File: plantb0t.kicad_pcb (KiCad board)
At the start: 2 copper layers, 50 x 50 mm, 61 parts, among them P1 CONN_02X09, P10 CONN_01X01, P11 CONN_01X01, P12 CONN_01X01, P13 CONN_01X01, P2 USB_OTG, P3 CONN_02X03, P4 CONN_01X02, P5 CONN_01X02, P6 CONN_01X02, P7 CONN_01X02, P8 CONN_01X04, P9 CONN_01X04, Q1 BS170, Q2 BS170, SW1 SWITCH_INV, U1 ESP-12, U10 BMP280, U11 74HC(T)4051, U12 LEDx2, U2 CP2102, U3 ZXCL5213V30H5CT-ND, U4 MCP4017 100K, U5 FXL6408, U6 FC6946010R, U7 FC6946010R, U8 MCP6001, U9 PSSI2021SAY

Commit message: Tweaking the ground plane and fixing missing traces
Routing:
- net /SENSORS: track 13.2 -> 44.4 mm, vias 0 -> 4
- net /GPIO_1: track 48.2 -> 28.3 mm
- net GND: track 50.4 -> 65.5 mm, vias 2 -> 4
- net +3V3: track 199.7 -> 205.8 mm, vias 8 -> 10
- added copper zone on B.Cu, net GND
- added copper zone on F.Cu, net GND
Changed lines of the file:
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@@
     (thickness 1.6)
     (drawings 8)
-    (tracks 735)
+    (tracks 768)
     (zones 0)
     (modules 61)
@@
   (gr_line (start 67 90) (end 113 90) (layer Edge.Cuts) (width 0.15))
   (gr_line (start 65 42) (end 65 88) (layer Edge.Cuts) (width 0.15))
+  (segment (start 87.75 78.95) (end 87.325736 78.95) (width 0.11) (layer F.Cu) (net 1))
+  (segment (start 87.325736 78.95) (end 86.025 78.95) (width 0.11) (layer F.Cu) (net 1))
+  (segment (start 84.275 79.825) (end 85.15 78.95) (width 0.11) (layer B.Cu) (net 1))
+  (segment (start 85.15 78.95) (end 87.75 78.95) (width 0.11) (layer B.Cu) (net 1))
+  (via (at 87.75 78.95) (size 0.6) (drill 0.4) (layers F.Cu B.Cu) (net 1))
+  (segment (start 83.13096 77.63) (end 83.99153 77.63) (width 0.11) (layer F.Cu) (net 1))
+  (segment (start 83.99153 77.63) (end 84.136531 77.775001) (width 0.11) (layer F.Cu) (net 1))
+  (via (at 84.275 79.825) (size 0.6) (drill 0.4) (layers F.Cu B.Cu) (net 1))
+  (segment (start 84.136531 77.775001) (end 84.136531 79.686531) (width 0.11) (layer F.Cu) (net 1))
+  (segment (start 84.136531 79.686531) (end 84.275 79.825) (width 0.11) (layer F.Cu) (net 1))
+  (segment (start 82.68 73.82) (end 82.04 73.82) (width 0.11) (layer F.Cu) (net 1))
+  (segment (start 82.04 73.82) (end 81.894999 73.674999) (width 0.11) (layer F.Cu) (net 1))
+  (segment (start 81.894999 73.674999) (end 81.894999 72.340999) (width 0.11) (layer F.Cu) (net 1))
+  (segment (start 81.894999 72.340999) (end 82.135997 72.100001) (width 0.11) (layer F.Cu) (net 1))
+  (segment (start 82.135997 72.100001) (end 84.600001 72.100001) (width 0.11) (layer F.Cu) (net 1))
+  (segment (start 86.2 72.6) (end 85.1 72.6) (width 0.11) (layer F.Cu) (net 1))
+  (segment (start 85.1 72.6) (end 84.9 72.4) (width 0.11) (layer F.Cu) (net 1))
   (segment (start 75.57 46.32) (end 75.57 45.18832) (width 0.175) (layer B.Cu) (net 1))
   (segment (start 75.57 45.18832) (end 74.88168 44.5) (width 0.175) (layer B.Cu) (net 1))
@@
   (segment (start 108.53 59.105) (end 108.53 59.175) (width 0.175) (layer F.Cu) (net 3))
   (segment (start 108.53 59.035) (end 108.53 59.105) (width 0.175) (layer F.Cu) (net 3))
+  (via (at 74.575 74.175) (size 0.6) (drill 0.4) (layers F.Cu B.Cu) (net 4))
+  (segment (start 75.17 74.77) (end 74.575 74.175) (width 0.11) (layer B.Cu) (net 4))
+  (segment (start 80.48 74.77) (end 75.17 74.77) (width 0.11) (layer B.Cu) (net 4))
+  (via (at 80.48 74.77) (size 0.6) (drill 0.4) (layers F.Cu B.Cu) (net 4))
   (segment (start 68.71 70) (end 68.71 71.221314) (width 0.25) (layer F.Cu) (net 4))
   (segment (start 68.71 71.221314) (end 70.138686 72.65) (width 0.25) (layer F.Cu) (net 4))
@@
   (segment (start 70.386401 63.243599) (end 71.25 62.38) (width 0.175) (layer F.Cu) (net 14))
   (segment (start 71.25 59.84) (end 72.113599 58.976401) (width 0.175) (layer F.Cu) (net 15))
-  (segment (start 80.922216 53.11317) (end 81.372896 52.66249) (width 0.175) (layer F.Cu) (net 15))
   (segment (start 72.113599 58.976401) (end 72.113599 58.140031) (width 0.175) (layer F.Cu) (net 15))
-  (segment (start 92.602692 55.5) (end 97.5 55.5) (width 0.175) (layer F.Cu) (net 15))
   (segment (start 72.113599 58.140031) (end 73.71363 56.54) (width 0.175) (layer F.Cu) (net 15))
   (segment (start 73.71363 56.54) (end 78.441411 56.54) (width 0.175) (layer F.Cu) (net 15))
   (segment (start 78.441411 56.54) (end 80.922216 54.059195) (width 0.175) (layer F.Cu) (net 15))
+  (segment (start 81.372896 52.66249) (end 84.865153 52.66249) (width 0.175) (layer F.Cu) (net 15))
+  (segment (start 84.865153 52.66249) (end 87.702663 55.5) (width 0.175) (layer F.Cu) (net 15))
   (segment (start 80.922216 54.059195) (end 80.922216 53.11317) (width 0.175) (layer F.Cu) (net 15))
-  (segment (start 81.372896 52.66249) (end 89.765182 52.66249) (width 0.175) (layer F.Cu) (net 15))
-  (segment (start 89.765182 52.66249) (end 92.602692 55.5) (width 0.175) (layer F.Cu) (net 15))
+  (segment (start 80.922216 53.11317) (end 81.372896 52.66249) (width 0.175) (layer F.Cu) (net 15))
+  (segment (start 87.702663 55.5) (end 97.5 55.5) (width 0.175) (layer F.Cu) (net 15))
   (segment (start 97.5 57.5) (end 98.084418 57.5) (width 0.175) (layer F.Cu) (net 16))
   (segment (start 78.887471 40.808899) (end 78.288899 41.407471) (width 0.175) (layer F.Cu) (net 16))
@@
   (segment (start 73.398904 55.151096) (end 72.113599 56.436401) (width 0.175) (layer F.Cu) (net 16))
   (segment (start 74.045269 45.651101) (end 73.398904 46.297466) (width 0.175) (layer F.Cu) (net 16))
-  (segment (start 108.45886 66.84) (end 106.9 66.84) (width 0.175) (layer F.Cu) (net 17))
   (segment (start 106.9 66.84) (end 100.991058 66.84) (width 0.175) (layer F.Cu) (net 17))
+  (segment (start 87.157888 55.87501) (end 84.782878 53.5) (width 0.175) (layer F.Cu) (net 17))
+  (segment (start 100.991058 66.84) (end 96.43 62.278942) (width 0.175) (layer F.Cu) (net 17))
+  (segment (start 96.43 62.278942) (end 96.43 58.04) (width 0.175) (layer F.Cu) (net 17))
+  (segment (start 96.43 58.04) (end 94.26501 55.87501) (width 0.175) (layer F.Cu) (net 17))
+  (segment (start 94.26501 55.87501) (end 87.157888 55.87501) (width 0.175) (layer F.Cu) (net 17))
+  (segment (start 84.782878 53.5) (end 83.5 53.5) (width 0.175) (layer F.Cu) (net 17))
+  (segment (start 108.45886 66.84) (end 106.9 66.84) (width 0.175) (layer F.Cu) (net 17))
   (segment (start 106.45 67.35) (end 106.45 66.99) (width 0.11) (layer F.Cu) (net 17))
   (segment (start 106.45 66.99) (end 106.6 66.84) (width 0.11) (layer F.Cu) (net 17))
@@
   (segment (start 67.464491 60.414382) (end 67.464491 58.545509) (width 0.175) (layer F.Cu) (net 17))
   (segment (start 67.464491 58.545509) (end 67.846401 58.163599) (width 0.175) (layer F.Cu) (net 17))
-  (segment (start 92.447357 55.875009) (end 90.072348 53.5) (width 0.175) (layer F.Cu) (net 17))
-  (segment (start 90.072348 53.5) (end 83.5 53.5) (width 0.175) (layer F.Cu) (net 17))
-  (segment (start 96.43 58.04) (end 94.26501 55.87501) (width 0.175) (layer F.Cu) (net 17))
-  (segment (start 94.26501 55.87501) (end 92.447357 55.875009) (width 0.175) (layer F.Cu) (net 17))
-  (segment (start 96.43 62.278942) (end 96.43 58.04) (width 0.175) (layer F.Cu) (net 17))
-  (segment (start 100.991058 66.84) (end 96.43 62.278942) (width 0.175) (layer F.Cu) (net 17))
   (segment (start 100.11252 57.471898) (end 98.084418 59.5) (width 0.175) (layer F.Cu) (net 18))
   (segment (start 100.11252 54.997757) (end 100.11252 57.471898) (width 0.175) (layer F.Cu) (net 18))
@@
   (segment (start 82.68 72.87) (end 83.385 72.87) (width 0.175) (layer F.Cu) (net 62))
   (segment (start 83.385 72.87) (end 83.93 73.415) (width 0.175) (layer F.Cu) (net 62))
-  (segment (start 71.25 70) (end 91.108598 70) (width 0.11) (layer B.Cu) (net 68))
   (segment (start 96.487569 75.378971) (end 104.946029 75.378971) (width 0.11) (layer B.Cu) (net 68))
   (segment (start 91.108598 70) (end 96.487569 75.378971) (width 0.11) (layer B.Cu) (net 68))
@@
   (segment (start 66 50.8) (end 67.12 49.68) (width 0.175) (layer F.Cu) (net 70))
   (segment (start 67.12 49.68) (end 68.71 49.68) (width 0.175) (layer F.Cu) (net 70))
+  (segment (start 85.8 73.15) (end 84.18 74.77) (width 0.11) (layer B.Cu) (net 71))
+  (segment (start 84.18 74.77) (end 82.68 74.77) (width 0.11) (layer B.Cu) (net 71))
+  (via (at 82.68 74.77) (size 0.6) (drill 0.4) (layers F.Cu B.Cu) (net 71))
+  (segment (start 85.8 69.075) (end 85.8 73.15) (width 0.11) (layer B.Cu) (net 71))
+  (segment (start 85.8 60.5) (end 85.8 69.075) (width 0.11) (layer F.Cu) (net 71))
+  (via (at 85.8 69.075) (size 0.6) (drill 0.4) (layers F.Cu B.Cu) (net 71))
+  (segment (start 88.775 57.525) (end 85.8 60.5) (width 0.11) (layer F.Cu) (net 71))
+  (segment (start 88.725 54.075) (end 88.725 57.475) (width 0.11) (layer B.Cu) (net 71))
+  (segment (start 88.725 57.475) (end 88.775 57.525) (width 0.11) (layer B.Cu) (net 71))
+  (via (at 88.775 57.525) (size 0.6) (drill 0.4) (layers F.Cu B.Cu) (net 71))
+  (segment (start 83.5 49.5) (end 84.15 49.5) (width 0.11) (layer F.Cu) (net 71))
+  (segment (start 84.15 49.5) (end 88.725 54.075) (width 0.11) (layer F.Cu) (net 71))
+  (via (at 88.725 54.075) (size 0.6) (drill 0.4) (layers F.Cu B.Cu) (net 71))
   (segment (start 82.68 75.27) (end 82.68 74.77) (width 0.175) (layer F.Cu) (net 71))
   (segment (start 82.035898 75.914102) (end 82.68 75.27) (width 0.175) (layer F.Cu) (net 71))
@@
       )
     )
+  )
+  (zone (net 1) (net_name GND) (layer F.Cu) (hatch edge 0.508)
+    (connect_pads (clearance 0.05))
+    (min_thickness 0.35)
+    (fill yes (arc_segments 16) (thermal_gap 0.005) (thermal_bridge_width 0.762))
+    (polygon
+      (pts
+        (xy 64.6 39.05) (xy 119.5 38) (xy 118.8 93.05) (xy 63.25 92.975)
+      )
+    )
+  )
+  (zone (net 1) (net_name GND) (layer B.Cu) (hatch edge 0.508)
+    (connect_pads (clearance 0.05))
+    (min_thickness 0.35)
+    (fill yes (arc_segments 16) (thermal_gap 0.005) (thermal_bridge_width 0.762))
+    (polygon
+      (pts
+        (xy 120.75 36.875) (xy 120.75 95.2) (xy 60.925 94.675) (xy 62.475 35.475) (xy 120.775 36.7)
+      )
+    )

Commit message: Finishing up board Revision A 2.0
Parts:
- I²C EXP 1: renamed from P8
- I²C EXP 2: renamed from P9
- moved FLASH 71.4 mm to (139.0, 90.4)
- moved R8 71.1 mm to (137.7, 81.3)
- moved D4 71.1 mm to (137.7, 84.9)
- moved R1 70.8 mm to (139.5, 84.5)
- moved D3 69.8 mm to (163.3, 92.7)
- moved U12 69.8 mm to (165.7, 89.2)
- moved AN_1 69.8 mm to (135.4, 120.8)
- moved AN_2 69.8 mm to (166.9, 120.8)
- moved AN_4 69.8 mm to (174.3, 109.2)
- moved C11 69.8 mm to (156.7, 99.7)
- moved C12 69.8 mm to (141.3, 102.8)
- moved C2 69.8 mm to (170.2, 82.5)
- moved C3 69.8 mm to (174.5, 81.0)
- moved C4 69.8 mm to (165.2, 75.8)
- moved C6 69.8 mm to (165.1, 98.0)
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- renumbered P7 to AN_1, P6 to AN_2, P5 to AN_3, P4 to AN_4, SW1 to FLASH, P3 to PROG, P2 to USB
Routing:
- net +5V: track 74.4 -> 81.5 mm
- net /GPIO_5: track 31.4 -> 34.1 mm
- net /GPIO_6: track 52.2 -> 54.4 mm
- net GND: track 65.5 -> 67.6 mm
- net /GPIO_7: track 54.9 -> 56.9 mm
- net /I2C_CLOCK: track 159.4 -> 158.3 mm
- net /SLEEP_CTRL: track 60.3 -> 59.2 mm
- net +3V3: track 205.8 -> 205.0 mm
- net /SENSORS: track 44.4 -> 45.2 mm
- net /CH_PD: track 22.3 -> 21.6 mm
- removed copper zone on F.Cu, net /PERM_3V3
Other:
- outline, holes or cut-outs redrawn
- board text added: "+5V"
- board text added: "10/2016"
- board text added: "3V3"
- board text added: "GND"
- board text added: "IO_2"
- board text added: "IO_3"
- board text added: "IO_4"
- board text added: "IO_5"
- board text added: "IO_6"
- board text added: "IO_7"
- board text added: "OUT_1"
- board text added: "Open Plantbot Rev A2"
- board text added: "P3V3"
- board text added: "RST"
- board text added: "SCL"
- board text added: "SDA"
- board text added: "SLP"

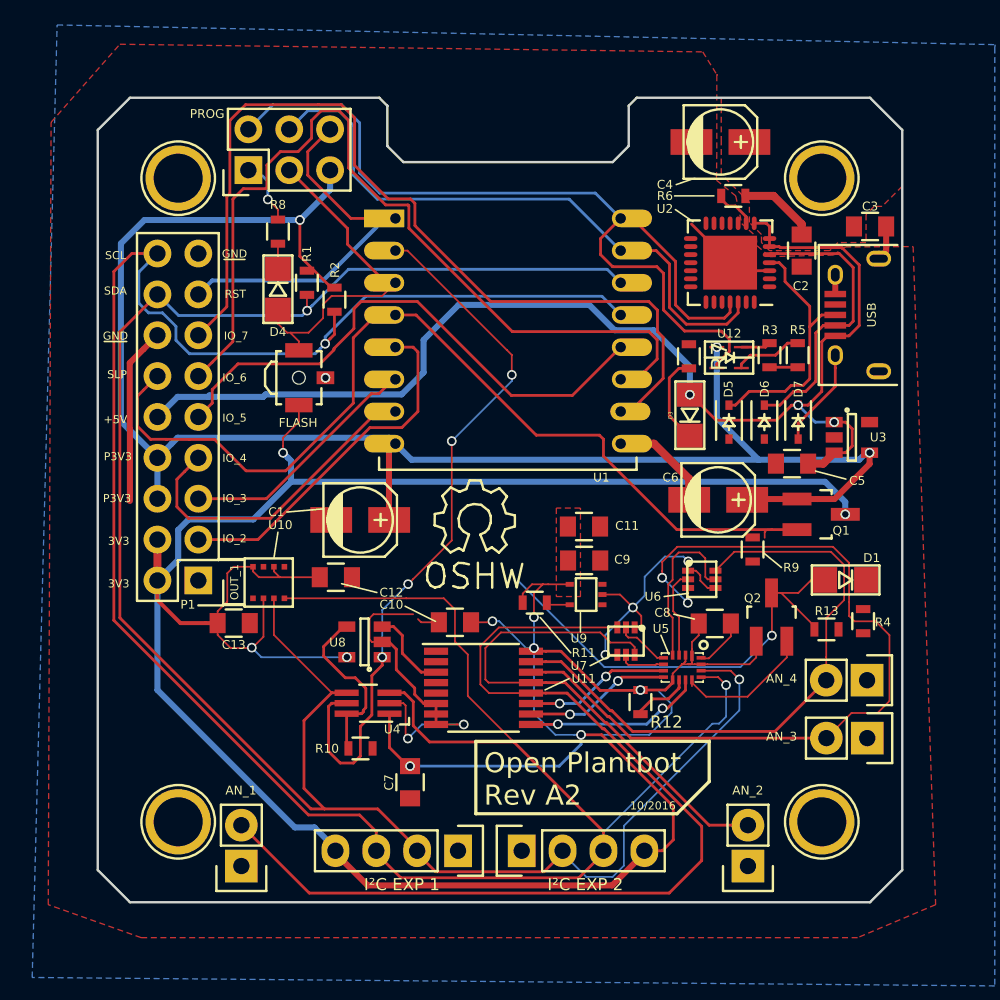
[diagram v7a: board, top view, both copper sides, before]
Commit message: Majorly updating the board. Moving some components. Changing the Plantbot logo \o/
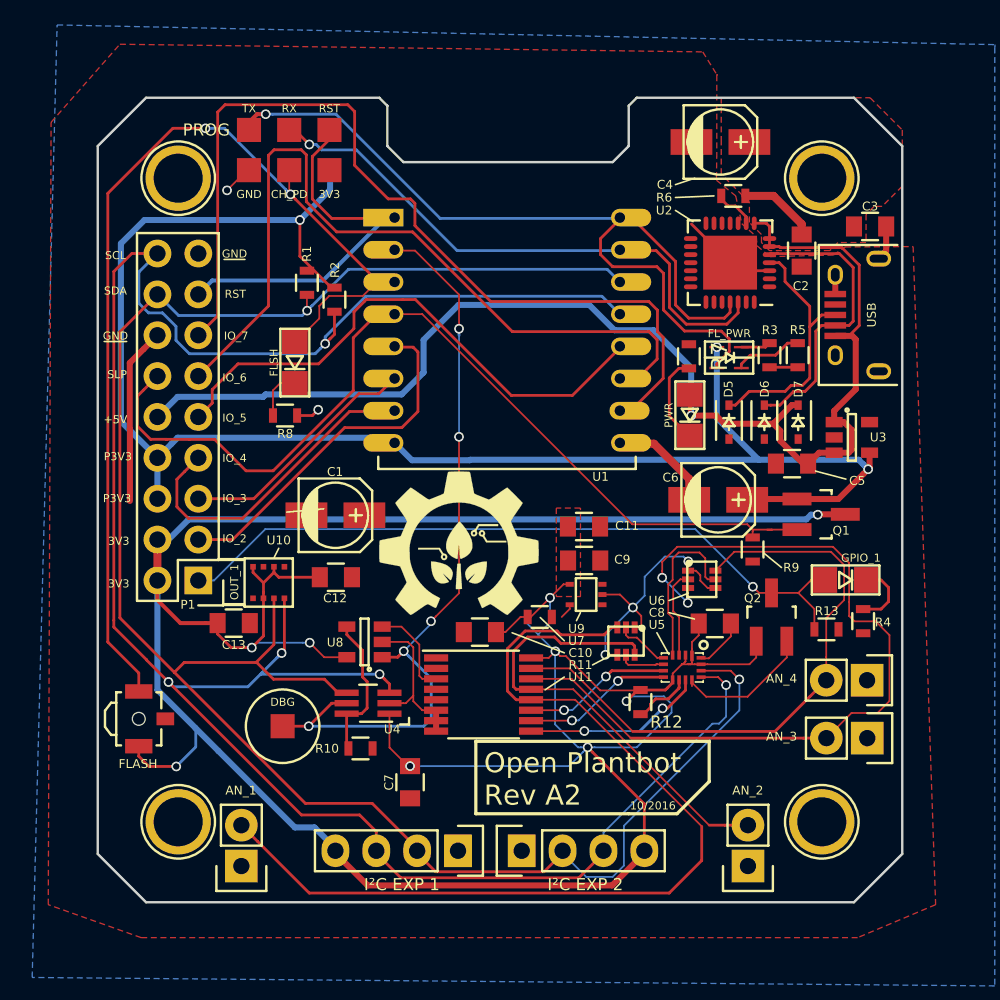
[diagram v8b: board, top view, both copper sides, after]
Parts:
- removed the PROG at (135.9, 77.5)
- removed REF**: Symbol_OSHW-Logo_SilkScreen, Symbols:Symbol_OSHW-Logo_SilkScreen
- added DBG: CONN_01X01, Connect:1pin, F.Cu at (138.0, 112.1)
- added G***: LOGO, plantbot_kicad:plantbot_icon, F.Cu at (148.9, 100.7)
- added G***: LOGO, eu_love:eu_love, B.Cu at (153.0, 103.5)
- added PROG: CONN_02X03, base_types:prog_6pin, F.Cu at (138.4, 77.5)
- moved FLASH 23.4 mm to (129.1, 111.6)
- moved R8 11.4 mm to (138.1, 92.8), turned to 180 degrees
- moved FLSH 4.68 mm to (138.8, 89.5), turned to 270 degrees
- moved C10 1.67 mm to (150.2, 106.2)
- moved C1 1.57 mm to (141.3, 99.0)
- moved R11 0.94 mm to (154.0, 105.3)
- moved U11 0.42 mm to (150.5, 110.1)
- moved U1 0.07 mm to (144.9, 80.5)
- renumbered D4 to FLSH, U12 to FL_PWR, D1 to GPIO_1, D3 to PWR
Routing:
- net /CH_PD: track 21.6 -> 65.3 mm, vias 0 -> 2
- net /I2C_CLOCK: track 158.3 -> 139.7 mm, vias 2 -> 5
- net GND: track 67.6 -> 49.1 mm, vias 4 -> 2
- net /GPIO_1: track 28.3 -> 45.4 mm
- net +3V3: track 205.0 -> 195.9 mm, vias 10 -> 9
- net +5V: track 81.5 -> 86.1 mm, vias 3 -> 1
- net /PERM_3V3: track 105.0 -> 100.6 mm
- net Net-(D1-Pad1): track 0.00 -> 4.23 mm
- net /GPIO_6: track 54.4 -> 50.4 mm
- net /Sensor Mounts/SENSE_C: track 32.6 -> 29.0 mm
- net /Sensor Mounts/SENSE_D: track 62.1 -> 59.1 mm
- net /FLASH_RX: track 38.2 -> 35.5 mm, vias 0 -> 1
- net /SENSORS: track 45.2 -> 47.5 mm, vias 4 -> 5
- net /FLASH_TX: track 56.7 -> 54.7 mm, vias 0 -> 1
- net Net-(R10-Pad1): track 10.8 -> 9.21 mm
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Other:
- outline, holes or cut-outs redrawn
- board text added: "CH_PD"
- board text added: "Made in EU"
- board text added: "RX"
- board text added: "TX"
